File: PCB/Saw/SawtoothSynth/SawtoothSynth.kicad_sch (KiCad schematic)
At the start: 39 parts, among them Q1 SS8550, U1 NE555D, U2 LM358, U3 LM386, U5 4017, U7 LD1117S50TR_SOT223

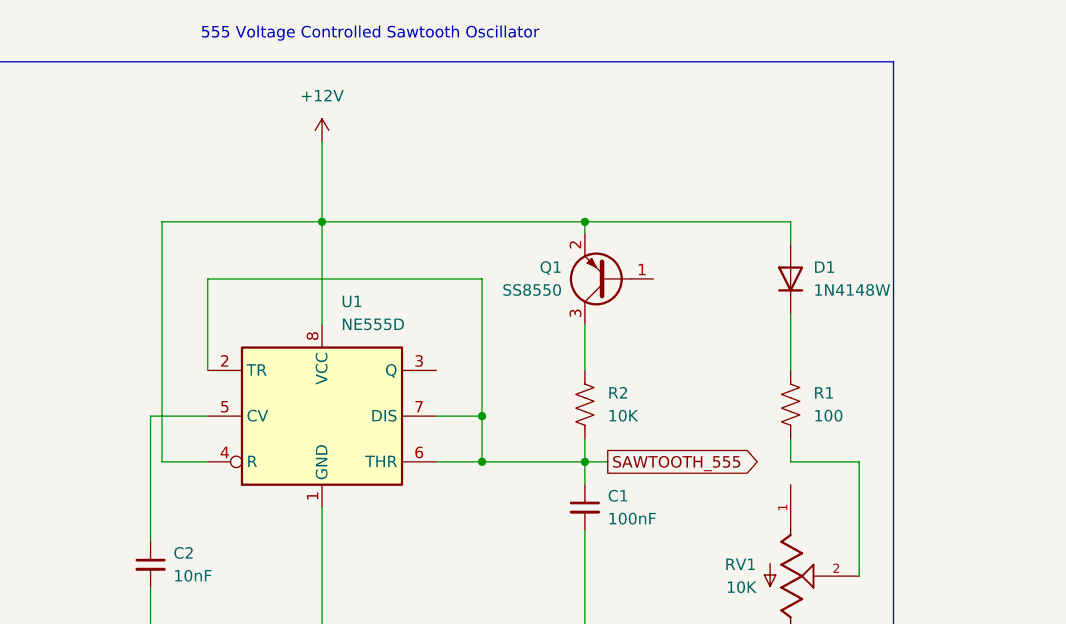
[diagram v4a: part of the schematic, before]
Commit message: Laid Out PCB  No DRC Errors
Finished laying out PCB, no DRC errors
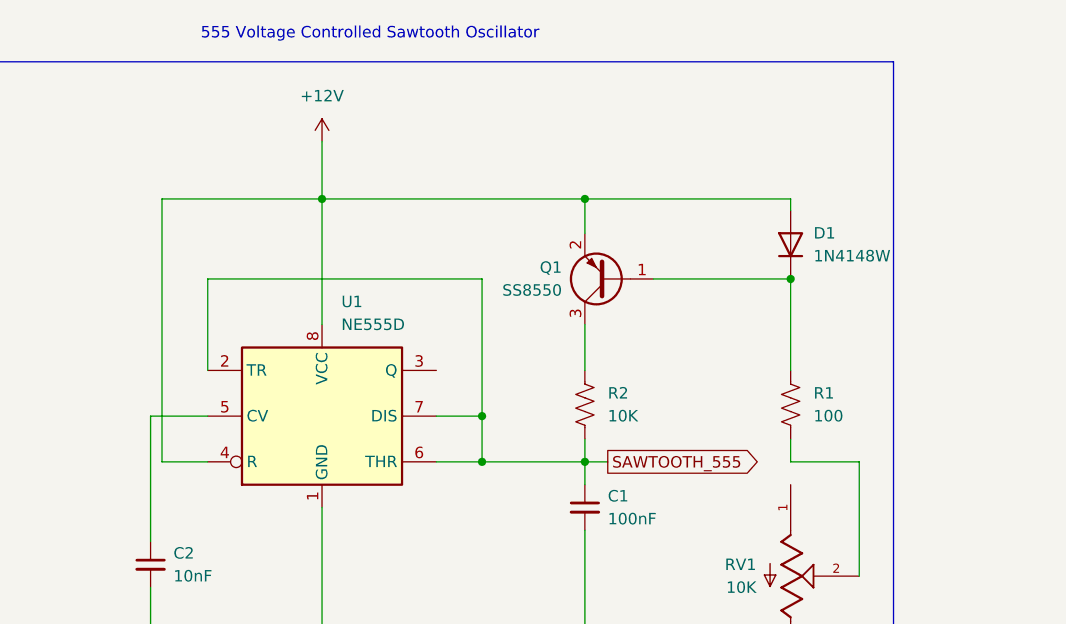
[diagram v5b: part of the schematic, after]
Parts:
- removed RoundDispTFT1: ~, CustomLibrary:1.28___Round_TFT, symbol Display:1.28{dblquote}_Round_TFT
- added RoundDispTFT1: ~, CustomLibrary:1.28___Round_TFT, symbol CustomLibrary:1.28{dblquote}_Round_TFT
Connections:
- net +5V: now also RoundDispTFT1.1 (Vcc)
- net GND: now also RoundDispTFT1.2 (GND)
- net SPI_CS: now also RoundDispTFT1.6 (CS)
- net SPI_DC: now also RoundDispTFT1.5 (DC)
- net SPI_MOSI: now also RoundDispTFT1.4 (SDA)
- net SPI_RST: now also RoundDispTFT1.7 (RST)
- net SPI_SCK: now also RoundDispTFT1.3 (SCL)
- net at Q1.1 (B): now also D1.1 (K), R1.1
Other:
- moved on the sheet: D1
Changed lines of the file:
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@@
 	)
 	(junction
+		(at 116.84 50.8)
+		(diameter 0)
+		(color 0 0 0 0)
+	)
+	(junction
 		(at 93.98 93.98)
 		(diameter 0)
@@
 	)
 	(junction
+		(at 93.98 41.91)
+		(diameter 0)
+		(color 0 0 0 0)
+	)
+	(junction
 		(at 64.77 93.98)
 		(diameter 0)
@@
 	)
 	(junction
-		(at 93.98 44.45)
+		(at 292.1 140.97)
 		(diameter 0)
 		(color 0 0 0 0)
@@
 	)
 	(junction
-		(at 64.77 44.45)
+		(at 64.77 41.91)
 		(diameter 0)
 		(color 0 0 0 0)
@@
 	)
 	(junction
-		(at 292.1 140.97)
-		(diameter 0)
-		(color 0 0 0 0)
-	)
-	(junction
 		(at 292.1 130.81)
 		(diameter 0)
@@
 	(wire
 		(pts
-			(xy 292.1 118.11) (xy 292.1 120.65)
+			(xy 236.22 140.97) (xy 243.84 140.97)
 		)
 		(stroke
@@
 	(wire
 		(pts
-			(xy 292.1 140.97) (xy 292.1 144.78)
+			(xy 292.1 118.11) (xy 292.1 120.65)
 		)
 		(stroke
@@
 	(wire
 		(pts
-			(xy 116.84 44.45) (xy 116.84 46.99)
+			(xy 116.84 41.91) (xy 116.84 43.18)
 		)
 		(stroke
@@
 	(wire
 		(pts
-			(xy 248.92 140.97) (xy 292.1 140.97)
-		)
-		(stroke
-			(width 0)
-			(type default)
-		)
-	)
-	(wire
-		(pts
 			(xy 82.55 66.04) (xy 82.55 71.12)
 		)
@@
 	(wire
 		(pts
-			(xy 93.98 45.72) (xy 93.98 44.45)
-		)
-		(stroke
-			(width 0)
-			(type default)
-		)
-	)
-	(wire
-		(pts
 			(xy 80.01 260.35) (xy 80.01 264.16)
 		)
@@
 	(wire
 		(pts
+			(xy 292.1 140.97) (xy 292.1 144.78)
+		)
+		(stroke
+			(width 0)
+			(type default)
+		)
+	)
+	(wire
+		(pts
 			(xy 80.01 264.16) (xy 77.47 264.16)
 		)
@@
 	(wire
 		(pts
-			(xy 116.84 54.61) (xy 116.84 60.96)
+			(xy 116.84 50.8) (xy 116.84 60.96)
 		)
 		(stroke
@@
 	(wire
 		(pts
-			(xy 46.99 44.45) (xy 64.77 44.45)
+			(xy 46.99 41.91) (xy 64.77 41.91)
 		)
 		(stroke
@@
 	(wire
 		(pts
-			(xy 64.77 55.88) (xy 64.77 44.45)
+			(xy 64.77 41.91) (xy 64.77 55.88)
 		)
 		(stroke
@@
 	(wire
 		(pts
-			(xy 64.77 35.56) (xy 64.77 44.45)
+			(xy 64.77 35.56) (xy 64.77 41.91)
 		)
 		(stroke
@@
 	(wire
 		(pts
-			(xy 330.2 144.78) (xy 341.63 144.78)
+			(xy 101.6 50.8) (xy 116.84 50.8)
 		)
 		(stroke
@@
 	(wire
 		(pts
-			(xy 236.22 130.81) (xy 264.16 130.81)
+			(xy 330.2 144.78) (xy 341.63 144.78)
 		)
 		(stroke
@@
 	(wire
 		(pts
-			(xy 113.03 237.49) (xy 116.84 237.49)
+			(xy 236.22 130.81) (xy 264.16 130.81)
 		)
 		(stroke
@@
 	(wire
 		(pts
-			(xy 284.48 120.65) (xy 292.1 120.65)
+			(xy 113.03 237.49) (xy 116.84 237.49)
 		)
 		(stroke
@@
 	(wire
 		(pts
-			(xy 236.22 140.97) (xy 243.84 140.97)
+			(xy 284.48 120.65) (xy 292.1 120.65)
 		)
 		(stroke
@@
 	(wire
 		(pts
-			(xy 46.99 71.12) (xy 46.99 44.45)
+			(xy 46.99 71.12) (xy 46.99 41.91)
 		)
 		(stroke
@@
 	(wire
 		(pts
-			(xy 93.98 44.45) (xy 116.84 44.45)
+			(xy 93.98 41.91) (xy 116.84 41.91)
 		)
 		(stroke
@@
 	(wire
 		(pts
+			(xy 248.92 140.97) (xy 292.1 140.97)
+		)
+		(stroke
+			(width 0)
+			(type default)
+		)
+	)
+	(wire
+		(pts
 			(xy 207.01 125.73) (xy 210.82 125.73)
 		)
@@
 	(wire
 		(pts
+			(xy 93.98 41.91) (xy 93.98 45.72)
+		)
+		(stroke
+			(width 0)
+			(type default)
+		)
+	)
+	(wire
+		(pts
 			(xy 93.98 71.12) (xy 93.98 73.66)
 		)
@@
 	(wire
 		(pts
-			(xy 93.98 44.45) (xy 64.77 44.45)
+			(xy 93.98 41.91) (xy 64.77 41.91)
 		)
 		(stroke
@@
 	)
 	(symbol
+		(lib_id "CustomLibrary:1.28{dblquote}_Round_TFT")
+		(at 344.17 127 0)
+		(unit 1)
+		(exclude_from_sim no)
+		(in_bom yes)
+		(on_board yes)
+		(dnp no)
+		(fields_autoplaced yes)
+		(property "Reference" "RoundDispTFT1"
+			(at 350.52 132.0799 0)
+			(effects
+				(font
+					(size 1.27 1.27)
+				)
+				(justify left)
+			)
+		)
+		(property "Value" "~"
+			(at 350.52 133.985 0)
+			(effects
+				(font
+					(size 1.27 1.27)
+				)
+				(justify left)
+			)
+		)
+		(property "Footprint" "CustomLibrary:1.28___Round_TFT"
+			(at 345.44 144.78 0)
+			(effects
+				(font
+					(size 1.27 1.27)
+				)
+				(hide yes)
+			)
+		)
+		(property "Datasheet" ""
+			(at 345.44 144.78 0)
+			(effects
+				(font
+					(size 1.27 1.27)
+				)
+				(hide yes)
+			)
+		)
+		(property "Description" ""
+			(at 345.44 144.78 0)
+			(effects
+				(font
+					(size 1.27 1.27)
+				)
+				(hide yes)
+			)
+		)
+		(pin "2"
+		)
+		(pin "6"
+		)
+		(pin "4"
+		)
+		(pin "7"
+		)
+		(pin "1"
+		)
+		(pin "5"
+		)
+		(pin "3"
+		)
+		(instances
+			(project ""
+				(path "/05357223-0530-467e-9944-156f1ca3379c"
+					(reference "RoundDispTFT1")
+					(unit 1)
+				)
+			)
+		)
+	)
+	(symbol
 		(lib_id "power:GNDREF")
 		(at 261.62 245.11 0)
@@
 	)
 	(symbol
-		(lib_id "Display:1.28{dblquote}_Round_TFT")
-		(at 344.17 127 0)
-		(unit 1)
-		(exclude_from_sim no)
-		(in_bom yes)
-		(on_board yes)
-		(dnp no)
-		(fields_autoplaced yes)
-		(property "Reference" "RoundDispTFT1"
-			(at 350.52 132.0799 0)
-			(effects
-				(font
-					(size 1.27 1.27)
-				)
-				(justify left)
-			)
-		)
-		(property "Value" "~"
-			(at 350.52 133.985 0)
-			(effects
-				(font
-					(size 1.27 1.27)
-				)
-				(justify left)
-			)
-		)
-		(property "Footprint" "CustomLibrary:1.28___Round_TFT"
-			(at 345.44 144.78 0)
-			(effects
-				(font
-					(size 1.27 1.27)
-				)
-				(hide yes)
-			)
-		)
-		(property "Datasheet" ""
-			(at 345.44 144.78 0)
-			(effects
-				(font
-					(size 1.27 1.27)
-				)
-				(hide yes)
-			)
-		)
-		(property "Description" ""
-			(at 345.44 144.78 0)
-			(effects
-				(font
-					(size 1.27 1.27)
-				)
-				(hide yes)
-			)
-		)
-		(pin "5"
-		)
-		(pin "4"
-		)
-		(pin "3"
-		)
-		(pin "7"
-		)
-		(pin "6"
-		)
-		(pin "2"
-		)
-		(pin "1"
-		)
-		(instances
-			(project ""
-				(path "/05357223-0530-467e-9944-156f1ca3379c"
-					(reference "RoundDispTFT1")
-					(unit 1)
-				)
-			)
-		)
-	)
-	(symbol
 		(lib_id "Device:R_US")
 		(at 292.1 148.59 0)
@@
 	(symbol
 		(lib_id "Diode:1N4148W")
-		(at 116.84 50.8 90)
+		(at 116.84 46.99 90)
 		(unit 1)
 		(exclude_from_sim no)
@@
 		(fields_autoplaced yes)
 		(property "Reference" "D1"
-			(at 119.38 49.5299 90)
+			(at 119.38 45.7199 90)
 			(effects
 				(font
@@
 		)
 		(property "Value" "1N4148W"
-			(at 119.38 52.0699 90)
+			(at 119.38 48.2599 90)
 			(effects
 				(font
@@
 		)
 		(property "Footprint" "Diode_SMD:D_SOD-123"
-			(at 121.285 50.8 0)
+			(at 121.285 46.99 0)
 			(effects
 				(font
@@
 		)
 		(property "Datasheet" "https://www.vishay.com/docs/85748/1n4148w.pdf"
-			(at 116.84 50.8 0)
+			(at 116.84 46.99 0)
 			(effects
 				(font
@@
 		)
 		(property "Description" "75V 0.15A Fast Switching Diode, SOD-123"
-			(at 116.84 50.8 0)
+			(at 116.84 46.99 0)
 			(effects
 				(font
@@
 		)
 		(property "Sim.Device" "D"
-			(at 116.84 50.8 0)
+			(at 116.84 46.99 0)
 			(effects
 				(font
@@
 		)
 		(property "Sim.Pins" "1=K 2=A"
-			(at 116.84 50.8 0)
+			(at 116.84 46.99 0)
 			(effects
 				(font

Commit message: Added Mounting Holes/Touch, Changed to 2-Layer Board
Added 3 standard M4 mounting holes for standoff and 1 M4 mounting hole connected to touch pin on micro.

I changed the board to a 2 layer since adding a solid copper pour for GND or PWR would ruin the transparent aesthetic
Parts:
- added MOUNTING1, MOUNTING2, MOUNTING3, TOUCH: MountingHole_Pad, MountingHole:MountingHole_4.3mm_M4_Pad_TopBottom, symbol Mechanical:MountingHole_Pad
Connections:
- net TOUCH: now also TOUCH.1
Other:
- note added: "Glass Mounting Holes"

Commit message: Added SPST Switch & DRC Fixes
Added SPST Toggle Switch to Schematic and PCB, Fixed Font DRC Errors & Courtyard Error For Silkscreen.

No DRC Errors
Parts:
- added SW1: SW_SPST, CustomLibrary:SW_SPST_Toggle, symbol Switch:SW_SPST
- renumbered TOUCH to TOUCH1
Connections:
- net +12V: now also SW1.2 (B); no longer C3.2
- new net: C3.2, SW1.1 (A)
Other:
- moved on the sheet: BATT1, C3
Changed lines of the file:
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@@
 	(rectangle
 		(start 15.24 26.67)
-		(end 128.27 130.81)
+		(end 132.08 130.81)
 		(stroke
 			(width 0)
@@
 	(rectangle
 		(start 252.73 224.79)
-		(end 274.32 252.73)
+		(end 274.32 266.7)
 		(stroke
 			(width 0)
@@
 	(wire
 		(pts
+			(xy 261.62 250.19) (xy 261.62 252.73)
+		)
+		(stroke
+			(width 0)
+			(type default)
+		)
+	)
+	(wire
+		(pts
 			(xy 80.01 264.16) (xy 77.47 264.16)
 		)
@@
 	(wire
 		(pts
+			(xy 261.62 243.84) (xy 261.62 245.11)
+		)
+		(stroke
+			(width 0)
+			(type default)
+		)
+	)
+	(wire
+		(pts
 			(xy 46.99 71.12) (xy 46.99 41.91)
 		)
@@
 	(wire
 		(pts
+			(xy 261.62 232.41) (xy 261.62 233.68)
+		)
+		(stroke
+			(width 0)
+			(type default)
+		)
+	)
+	(wire
+		(pts
 			(xy 45.72 66.04) (xy 45.72 80.01)
 		)
@@
 	(symbol
 		(lib_id "power:GNDREF")
-		(at 261.62 245.11 0)
+		(at 261.62 260.35 0)
 		(unit 1)
 		(exclude_from_sim no)
@@
 		(fields_autoplaced yes)
 		(property "Reference" "#PWR07"
-			(at 261.62 251.46 0)
+			(at 261.62 266.7 0)
 			(effects
 				(font
@@
 		)
 		(property "Value" "GND"
-			(at 261.62 250.19 0)
+			(at 261.62 265.43 0)
 			(effects
 				(font
@@
 		)
 		(property "Footprint" ""
-			(at 261.62 245.11 0)
+			(at 261.62 260.35 0)
 			(effects
 				(font
@@
 		)
 		(property "Datasheet" ""
-			(at 261.62 245.11 0)
+			(at 261.62 260.35 0)
 			(effects
 				(font
@@
 		)
 		(property "Description" "Power symbol creates a global label with name \"GNDREF\" , reference supply ground"
-			(at 261.62 245.11 0)
+			(at 261.62 260.35 0)
 			(effects
 				(font
@@
 	(symbol
 		(lib_id "Device:C_Small")
-		(at 261.62 234.95 180)
+		(at 261.62 247.65 180)
 		(unit 1)
 		(exclude_from_sim no)
@@
 		(fields_autoplaced yes)
 		(property "Reference" "C3"
-			(at 264.16 233.6735 0)
+			(at 264.16 246.3735 0)
 			(effects
 				(font
@@
 		)
 		(property "Value" "10nF"
-			(at 264.16 236.2135 0)
+			(at 264.16 248.9135 0)
 			(effects
 				(font
@@
 		)
 		(property "Footprint" "Capacitor_SMD:C_0805_2012Metric"
-			(at 261.62 234.95 0)
+			(at 261.62 247.65 0)
 			(effects
 				(font
@@
 		)
 		(property "Datasheet" "~"
-			(at 261.62 234.95 0)
+			(at 261.62 247.65 0)
 			(effects
 				(font
@@
 		)
 		(property "Description" "Unpolarized capacitor, small symbol"
-			(at 261.62 234.95 0)
+			(at 261.62 247.65 0)
 			(effects
 				(font
@@
 	)
 	(symbol
+		(lib_id "Switch:SW_SPST")
+		(at 261.62 238.76 90)
+		(unit 1)
+		(exclude_from_sim no)
+		(in_bom yes)
+		(on_board yes)
+		(dnp no)
+		(fields_autoplaced yes)
+		(property "Reference" "SW1"
+			(at 262.89 237.4899 90)
+			(effects
+				(font
+					(size 1.27 1.27)
+				)
+				(justify right)
+			)
+		)
+		(property "Value" "SW_SPST"
+			(at 262.89 240.0299 90)
+			(effects
+				(font
+					(size 1.27 1.27)
+				)
+				(justify right)
+			)
+		)
+		(property "Footprint" "CustomLibrary:SW_SPST_Toggle"
+			(at 261.62 238.76 0)
+			(effects
+				(font
+					(size 1.27 1.27)
+				)
+				(hide yes)
+			)
+		)
+		(property "Datasheet" "~"
+			(at 261.62 238.76 0)
+			(effects
+				(font
+					(size 1.27 1.27)
+				)
+				(hide yes)
+			)
+		)
+		(property "Description" "Single Pole Single Throw (SPST) switch"
+			(at 261.62 238.76 0)
+			(effects
+				(font
+					(size 1.27 1.27)
+				)
+				(hide yes)
+			)
+		)
+		(pin "2"
+		)
+		(pin "1"
+		)
+		(instances
+			(project ""
+				(path "/05357223-0530-467e-9944-156f1ca3379c"
+					(reference "SW1")
+					(unit 1)
+				)
+			)
+		)
+	)
+	(symbol
 		(lib_id "power:+12V")
 		(at 223.52 109.22 0)
@@
 	(symbol
 		(lib_id "CustomLibrary:BH23APC")
-		(at 257.81 241.3 270)
+		(at 257.81 256.54 270)
 		(unit 1)
 		(exclude_from_sim no)
@@
 		(fields_autoplaced yes)
 		(property "Reference" "BATT1"
-			(at 265.43 240.0934 90)
+			(at 265.43 255.3334 90)
 			(effects
 				(font
@@
 		)
 		(property "Value" "~"
-			(at 265.43 241.9985 90)
+			(at 265.43 257.2385 90)
 			(effects
 				(font
@@
 		)
 		(property "Footprint" "CustomLibrary:BH23APC"
-			(at 257.81 241.3 0)
+			(at 257.81 256.54 0)
 			(effects
 				(font
@@
 		)
 		(property "Datasheet" ""
-			(at 257.81 241.3 0)
+			(at 257.81 256.54 0)
 			(effects
 				(font
@@
 		)
 		(property "Description" ""
-			(at 257.81 241.3 0)
+			(at 257.81 256.54 0)
 			(effects
 				(font
@@
 		(on_board yes)
 		(dnp no)
-		(property "Reference" "TOUCH"
+		(property "Reference" "TOUCH1"
 			(at 208.28 187.96 0)
 			(effects
@@
 			(project "SawtoothSynth"
 				(path "/05357223-0530-467e-9944-156f1ca3379c"
-					(reference "TOUCH")
+					(reference "TOUCH1")
 					(unit 1)
 				)

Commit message: Updated Schematic for 10865 Battery
Changed BATT1 footprint to 18650PC Battery Holder 1043P
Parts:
- BATT1: footprint CustomLibrary:BH23APC -> CustomLibrary:18650PC Battery Holder 1043P
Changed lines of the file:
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@@
 			)
 		)
-		(property "Footprint" "CustomLibrary:BH23APC"
+		(property "Footprint" "CustomLibrary:18650PC Battery Holder 1043P"
 			(at 257.81 256.54 0)
 			(effects
